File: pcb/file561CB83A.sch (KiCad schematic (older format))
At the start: 44 parts

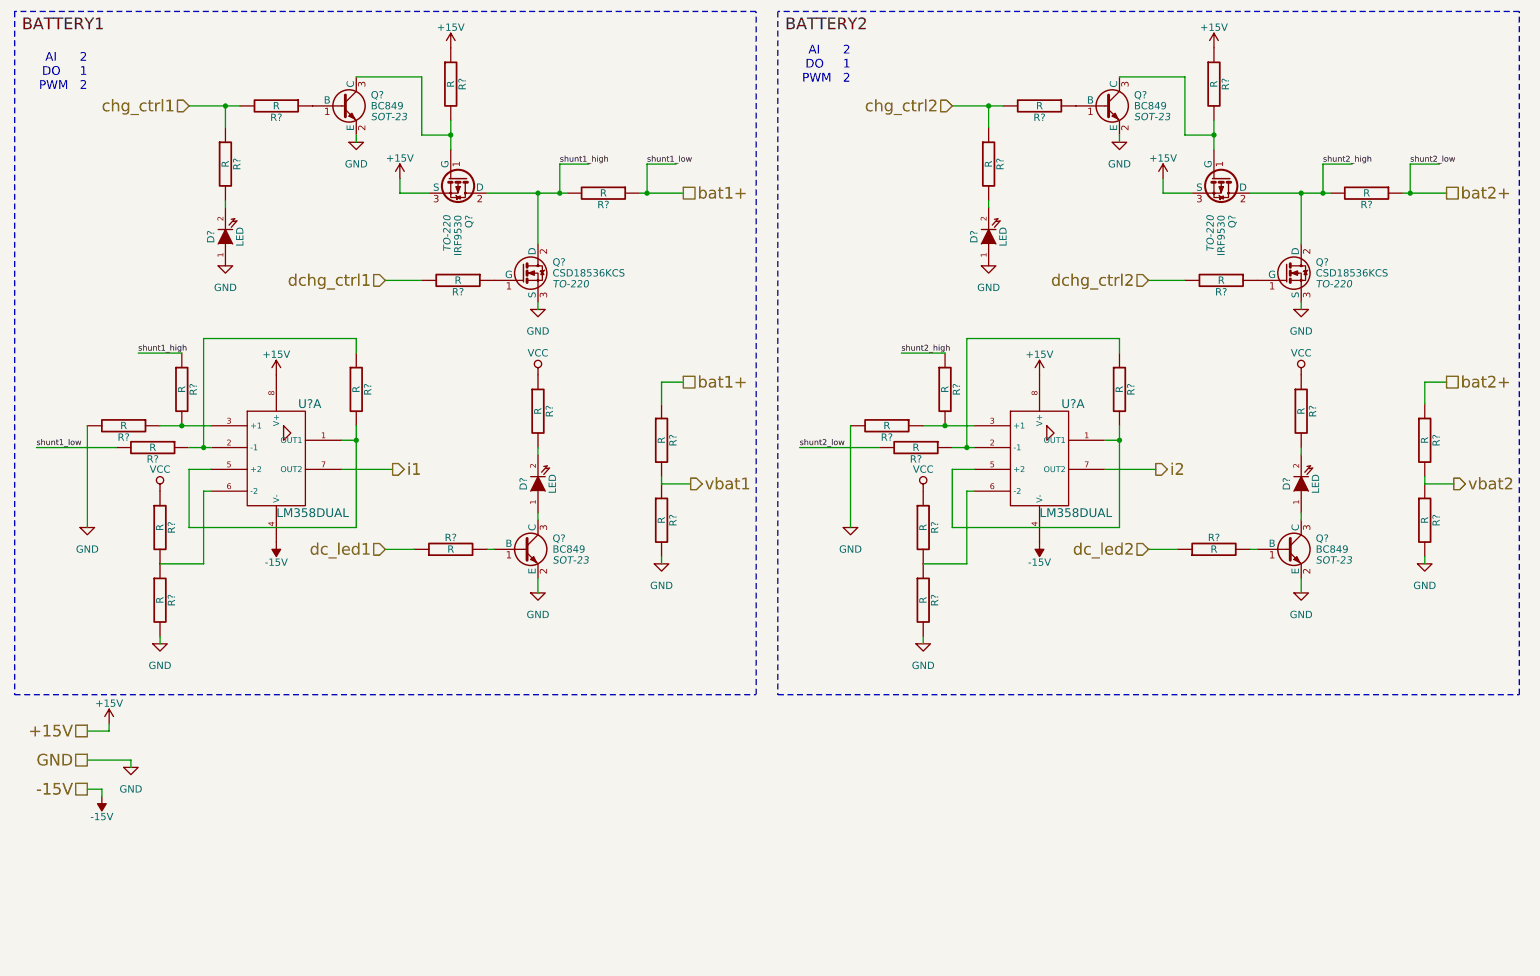
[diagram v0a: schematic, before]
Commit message: updated schematics
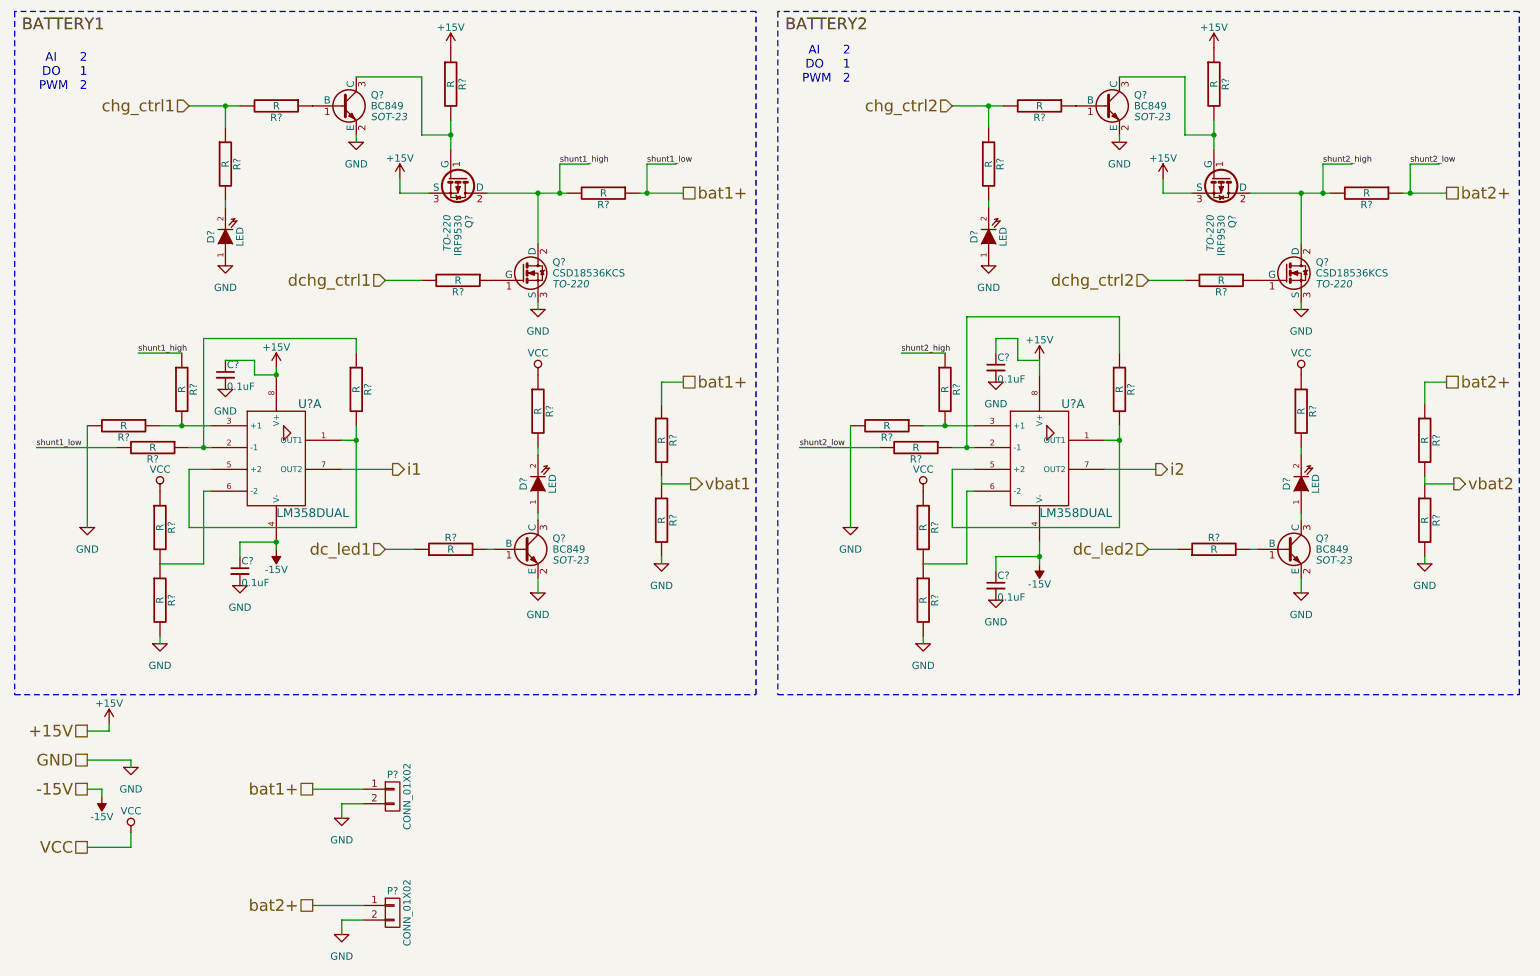
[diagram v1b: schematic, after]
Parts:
- added C? (x4): 0.1uF, symbol C_Small
- added P? (x2): CONN_01X02, symbol CONN_01X02
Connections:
- wire segments 100 -> 123

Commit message: starting on layout
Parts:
- C13, C14, C15, C16: renamed from C?; footprint (none) -> Capacitors_SMD:C_0805_HandSoldering
- D1, D2, D3, D4: renamed from D?; footprint (none) -> LEDs:LED-0805
- P8, P9: renamed from P?; footprint (none) -> Pin_Headers:Pin_Header_Straight_1x02
- Q2, Q5, Q6, Q9: renamed from Q?; footprint SOT-23 -> TO_SOT_Packages_SMD:SOT-23_Handsoldering
- Q3, Q4, Q7, Q8: renamed from Q?; footprint TO-220 -> Power_Integrations:TO-220
- R10, R20, R21, R22, R23, R24, R25, R29, R35, R36, R7, R8, R9: renamed from R?; footprint (none) -> Resistors_ThroughHole:Resistor_Horizontal_RM10mm
- R11, R14, R26: renamed from R?; footprint (none) -> Resistors_ThroughHole:Resistor_Horizontal_RM10mm; symbol R-RESCUE-BatAger -> R
- R12: renamed from R?; footprint (none) -> Resistors_SMD:R_0805_HandSoldering; Part # (none) -> RC0805JR-07 200R
- R13, R16, R17, R18: renamed from R?; value R -> 200; footprint (none) -> Resistors_SMD:R_0805_HandSoldering; Part # (none) -> RC0805JR-07 200R
- R15, R27, R28, R30, R31, R32, R33: renamed from R?; footprint (none) -> Resistors_SMD:R_0805_HandSoldering
- R19, R34: renamed from R?; footprint (none) -> Resistors_SMD:R_2512_HandSoldering
- U2, U3: renamed from U?; footprint (none) -> Housings_SOIC:SOIC-8_3.9x4.9mm_Pitch1.27mm
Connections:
- net at R23.1, R29.1: now also U3.6 (-2); no longer U3.2 (-1)
- net at R22.1, R26.2: now also U3.5 (+2); no longer U3.3 (+1)
- new net: R29.2, U3.5 (+2), U3.7 (OUT2)

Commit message: trace complete (maybe!)
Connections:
- net at R29.2, U3.5 (+2): now also U3.1 (OUT1); no longer U3.7 (OUT2)
- net at R22.1, R26.2: now also U3.3 (+1); no longer U3.5 (+2)
- net at R23.1, R29.1: now also U3.2 (-1); no longer U3.6 (-2)
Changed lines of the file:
@@
 $Comp
 L LM358Dual U3
-U 2 1 561D0E41
+U 1 1 561D0E41
 P 7650 3500
 F 0 "U3" H 7800 3750 60  0000 L CNN
@@
 F 2 "Housings_SOIC:SOIC-8_3.9x4.9mm_Pitch1.27mm" H 7650 3500 60  0001 C CNN
 F 3 "" H 7650 3500 60  0000 C CNN
-	2    7650 3500
+	1    7650 3500
 	1    0    0    -1
 $EndComp

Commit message: Production candidate - passes DRC.
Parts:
- R10, R11, R14, R20, R21, R22, R23, R24, R25, R26, R29, R35, R36, R7, R8, R9: footprint Resistors_ThroughHole:Resistor_Horizontal_RM10mm -> Custom Footprints:Resistor_Horizontal_RM10mm
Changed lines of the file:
@@
 F 0 "R21" V 5130 4050 50  0000 C CNN
 F 1 "R" V 5050 4050 50  0000 C CNN
-F 2 "Resistors_ThroughHole:Resistor_Horizontal_RM10mm" V 4980 4050 30  0001 C CNN
+F 2 "Custom Footprints:Resistor_Horizontal_RM10mm" V 4980 4050 30  0001 C CNN
 F 3 "" H 5050 4050 30  0000 C CNN
 	1    5050 4050
@@
 F 0 "R20" V 5130 3500 50  0000 C CNN
 F 1 "R" V 5050 3500 50  0000 C CNN
-F 2 "Resistors_ThroughHole:Resistor_Horizontal_RM10mm" V 4980 3500 30  0001 C CNN
+F 2 "Custom Footprints:Resistor_Horizontal_RM10mm" V 4980 3500 30  0001 C CNN
 F 3 "" H 5050 3500 30  0000 C CNN
 	1    5050 3500
@@
 F 0 "R11" V 1830 3150 50  0000 C CNN
 F 1 "R" V 1750 3150 50  0000 C CNN
-F 2 "Resistors_ThroughHole:Resistor_Horizontal_RM10mm" V 1680 3150 30  0001 C CNN
+F 2 "Custom Footprints:Resistor_Horizontal_RM10mm" V 1680 3150 30  0001 C CNN
 F 3 "" H 1750 3150 30  0000 C CNN
 	1    1750 3150
@@
 F 0 "R7" V 1430 3400 50  0000 C CNN
 F 1 "R" V 1350 3400 50  0000 C CNN
-F 2 "Resistors_ThroughHole:Resistor_Horizontal_RM10mm" V 1280 3400 30  0001 C CNN
+F 2 "Custom Footprints:Resistor_Horizontal_RM10mm" V 1280 3400 30  0001 C CNN
 F 3 "" H 1350 3400 30  0000 C CNN
 	1    1350 3400
@@
 F 0 "R8" V 1630 3550 50  0000 C CNN
 F 1 "R" V 1550 3550 50  0000 C CNN
-F 2 "Resistors_ThroughHole:Resistor_Horizontal_RM10mm" V 1480 3550 30  0001 C CNN
+F 2 "Custom Footprints:Resistor_Horizontal_RM10mm" V 1480 3550 30  0001 C CNN
 F 3 "" H 1550 3550 30  0000 C CNN
 	1    1550 3550
@@
 F 0 "R14" V 3030 3150 50  0000 C CNN
 F 1 "R" V 2950 3150 50  0000 C CNN
-F 2 "Resistors_ThroughHole:Resistor_Horizontal_RM10mm" V 2880 3150 30  0001 C CNN
+F 2 "Custom Footprints:Resistor_Horizontal_RM10mm" V 2880 3150 30  0001 C CNN
 F 3 "" H 2950 3150 30  0000 C CNN
 	1    2950 3150
@@
 F 0 "R9" V 1680 4100 50  0000 C CNN
 F 1 "R" V 1600 4100 50  0000 C CNN
-F 2 "Resistors_ThroughHole:Resistor_Horizontal_RM10mm" V 1530 4100 30  0001 C CNN
+F 2 "Custom Footprints:Resistor_Horizontal_RM10mm" V 1530 4100 30  0001 C CNN
 F 3 "" H 1600 4100 30  0000 C CNN
 	1    1600 4100
@@
 F 0 "R10" V 1680 4600 50  0000 C CNN
 F 1 "R" V 1600 4600 50  0000 C CNN
-F 2 "Resistors_ThroughHole:Resistor_Horizontal_RM10mm" V 1530 4600 30  0001 C CNN
+F 2 "Custom Footprints:Resistor_Horizontal_RM10mm" V 1530 4600 30  0001 C CNN
 F 3 "" H 1600 4600 30  0000 C CNN
 	1    1600 4600
@@
 F 0 "R36" V 10380 4050 50  0000 C CNN
 F 1 "R" V 10300 4050 50  0000 C CNN
-F 2 "Resistors_ThroughHole:Resistor_Horizontal_RM10mm" V 10230 4050 30  0001 C CNN
+F 2 "Custom Footprints:Resistor_Horizontal_RM10mm" V 10230 4050 30  0001 C CNN
 F 3 "" H 10300 4050 30  0000 C CNN
 	1    10300 4050
@@
 F 0 "R35" V 10380 3500 50  0000 C CNN
 F 1 "R" V 10300 3500 50  0000 C CNN
-F 2 "Resistors_ThroughHole:Resistor_Horizontal_RM10mm" V 10230 3500 30  0001 C CNN
+F 2 "Custom Footprints:Resistor_Horizontal_RM10mm" V 10230 3500 30  0001 C CNN
 F 3 "" H 10300 3500 30  0000 C CNN
 	1    10300 3500
@@
 F 0 "R26" V 7080 3150 50  0000 C CNN
 F 1 "R" V 7000 3150 50  0000 C CNN
-F 2 "Resistors_ThroughHole:Resistor_Horizontal_RM10mm" V 6930 3150 30  0001 C CNN
+F 2 "Custom Footprints:Resistor_Horizontal_RM10mm" V 6930 3150 30  0001 C CNN
 F 3 "" H 7000 3150 30  0000 C CNN
 	1    7000 3150
@@
 F 0 "R22" V 6680 3400 50  0000 C CNN
 F 1 "R" V 6600 3400 50  0000 C CNN
-F 2 "Resistors_ThroughHole:Resistor_Horizontal_RM10mm" V 6530 3400 30  0001 C CNN
+F 2 "Custom Footprints:Resistor_Horizontal_RM10mm" V 6530 3400 30  0001 C CNN
 F 3 "" H 6600 3400 30  0000 C CNN
 	1    6600 3400
@@
 F 0 "R23" V 6880 3550 50  0000 C CNN
 F 1 "R" V 6800 3550 50  0000 C CNN
-F 2 "Resistors_ThroughHole:Resistor_Horizontal_RM10mm" V 6730 3550 30  0001 C CNN
+F 2 "Custom Footprints:Resistor_Horizontal_RM10mm" V 6730 3550 30  0001 C CNN
 F 3 "" H 6800 3550 30  0000 C CNN
 	1    6800 3550
@@
 F 0 "R29" V 8280 3150 50  0000 C CNN
 F 1 "R" V 8200 3150 50  0000 C CNN
-F 2 "Resistors_ThroughHole:Resistor_Horizontal_RM10mm" V 8130 3150 30  0001 C CNN
+F 2 "Custom Footprints:Resistor_Horizontal_RM10mm" V 8130 3150 30  0001 C CNN
 F 3 "" H 8200 3150 30  0000 C CNN
 	1    8200 3150
@@
 F 0 "R24" V 6930 4100 50  0000 C CNN
 F 1 "R" V 6850 4100 50  0000 C CNN
-F 2 "Resistors_ThroughHole:Resistor_Horizontal_RM10mm" V 6780 4100 30  0001 C CNN
+F 2 "Custom Footprints:Resistor_Horizontal_RM10mm" V 6780 4100 30  0001 C CNN
 F 3 "" H 6850 4100 30  0000 C CNN
 	1    6850 4100
@@
 F 0 "R25" V 6930 4600 50  0000 C CNN
 F 1 "R" V 6850 4600 50  0000 C CNN
-F 2 "Resistors_ThroughHole:Resistor_Horizontal_RM10mm" V 6780 4600 30  0001 C CNN
+F 2 "Custom Footprints:Resistor_Horizontal_RM10mm" V 6780 4600 30  0001 C CNN
 F 3 "" H 6850 4600 30  0000 C CNN
 	1    6850 4600
